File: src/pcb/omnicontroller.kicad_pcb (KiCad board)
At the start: 2 copper layers, 124.5 x 68.6 mm, 51 parts, among them J1 G-Switch GT-USB-7010ASV, U1 RP2040, U2 NCP1117ST33T3G, U3 W25Q128JVSIM, X1 SW_Omron_B3FS-1000P, Y1 ABM8-272-T3, Y2 SW_Omron_B3FS-1000P

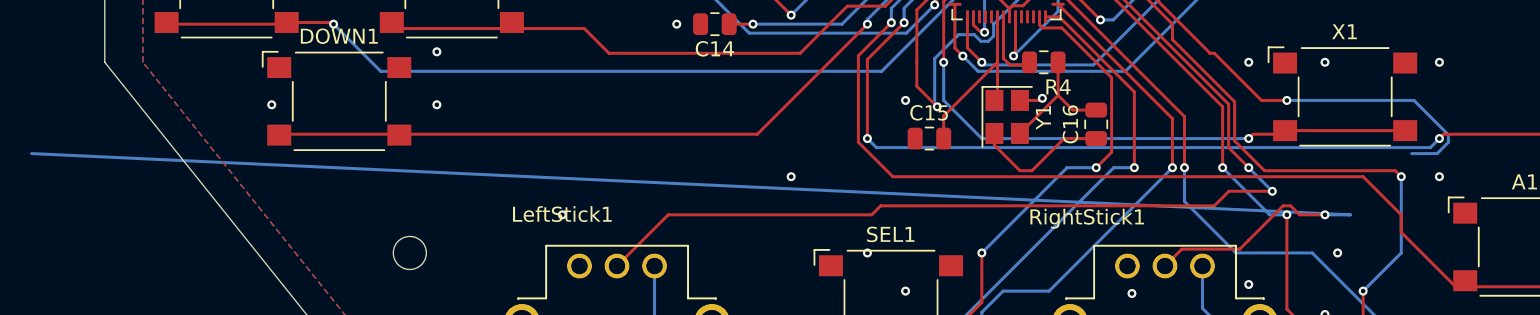
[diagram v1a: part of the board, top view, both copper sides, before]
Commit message: add RKJXV122400 footprint
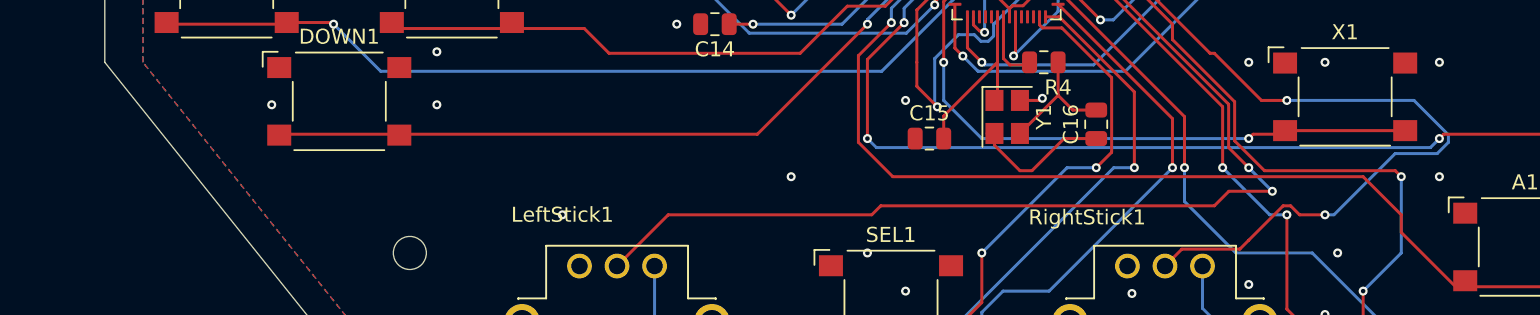
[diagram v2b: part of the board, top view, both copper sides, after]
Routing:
- net GP29: track 137.1 -> 54.9 mm
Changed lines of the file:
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@@
 			(drillshape 0)
 			(scaleselection 1)
-			(outputdirectory "../fabrication/v1.0.2/gerber/")
+			(outputdirectory "../../release/pcb/")
 		)
 	)
@@
 			(size 1 2.1)
 			(drill oval 0.6 1.7)
+			(property pad_prop_heatsink)
 			(layers "*.Cu" "*.Mask")
 			(remove_unused_layers no)
@@
 			(size 1 1.8)
 			(drill oval 0.6 1.4)
+			(property pad_prop_heatsink)
 			(layers "*.Cu" "*.Mask")
 			(remove_unused_layers no)
@@
 			(size 1 2.1)
 			(drill oval 0.6 1.7)
+			(property pad_prop_heatsink)
 			(layers "*.Cu" "*.Mask")
 			(remove_unused_layers no)
@@
 			(size 1 1.8)
 			(drill oval 0.6 1.4)
+			(property pad_prop_heatsink)
 			(layers "*.Cu" "*.Mask")
 			(remove_unused_layers no)
@@
 		)
 		(embedded_fonts no)
-		(model "${KICAD6_3DMODEL_DIR}/Connector_USB.3dshapes/USB_C_Receptacle_G-Switch_GT-USB-7010ASV.wrl"
+		(model "${KICAD9_3DMODEL_DIR}/Connector_USB.3dshapes/USB_C_Receptacle_G-Switch_GT-USB-7010ASV.wrl"
 			(offset
 				(xyz 0 0 0)
@@
 	(segment
 		(start 145.38 81.031471)
-		(end 145.38 81.528529)
+		(end 143.088529 78.74)
 		(width 0.2)
 		(layer "B.Cu")
@@
 	)
 	(segment
-		(start 143.088529 78.74)
-		(end 145.38 81.031471)
+		(start 144.628529 82.28)
+		(end 145.38 81.528529)
 		(width 0.2)
 		(layer "B.Cu")
@@
 	)
 	(segment
-		(start 144.628529 82.28)
-		(end 142.931471 82.28)
+		(start 143.088529 78.74)
+		(end 134.62 78.74)
 		(width 0.2)
 		(layer "B.Cu")
@@
 	)
 	(segment
-		(start 134.62 78.74)
-		(end 143.088529 78.74)
+		(start 145.38 81.528529)
+		(end 145.38 81.031471)
 		(width 0.2)
 		(layer "B.Cu")
@@
 	)
 	(segment
-		(start 145.38 81.528529)
-		(end 144.628529 82.28)
+		(start 137.75319 86.36)
+		(end 141.83319 82.28)
 		(width 0.2)
 		(layer "B.Cu")
@@
 	)
 	(segment
-		(start 51 82.28)
-		(end 138.851471 86.36)
+		(start 141.83319 82.28)
+		(end 144.628529 82.28)
 		(width 0.2)
 		(layer "B.Cu")
@@
 	)
 	(segment
-		(start 138.851471 86.36)
-		(end 137.16 86.36)
+		(start 137.16 86.36)
+		(end 137.75319 86.36)
 		(width 0.2)
 		(layer "B.Cu")

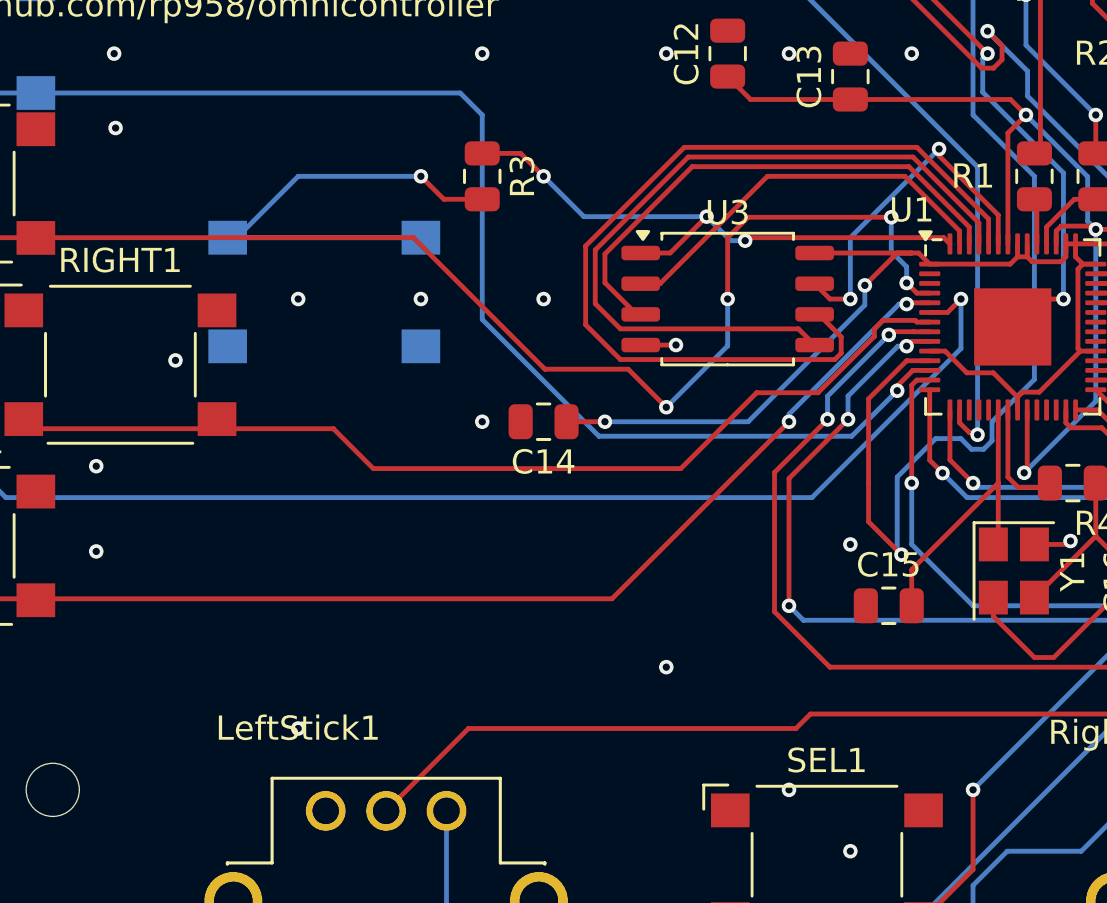
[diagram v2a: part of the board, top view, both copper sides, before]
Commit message: fix some drc warnings
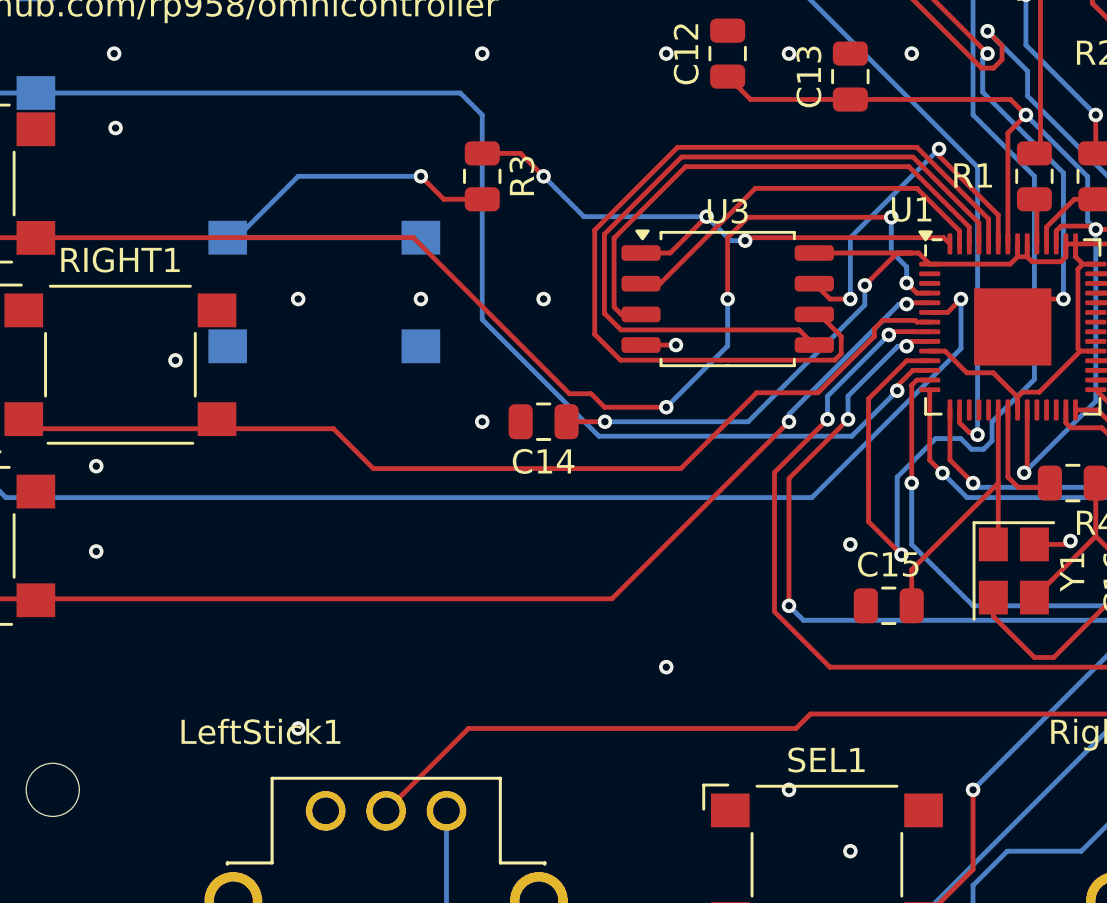
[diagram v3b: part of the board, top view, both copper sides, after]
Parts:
- U3: footprint Package_SO:SOIC-8_5.23x5.23mm_P1.27mm -> Package_SO:SOIC-8_5.3x5.3mm_P1.27mm

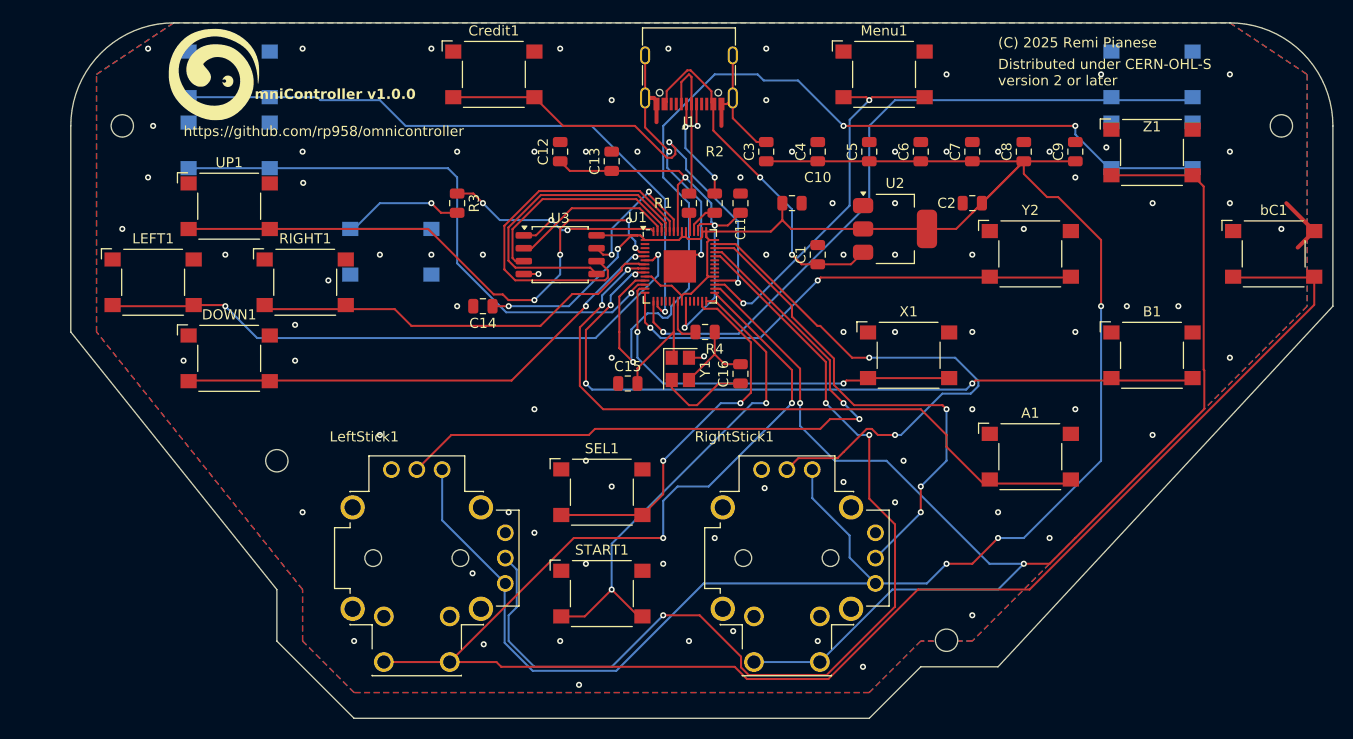
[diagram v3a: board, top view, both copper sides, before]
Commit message: move L1,L2, R1 and R2 buttons to top side
replace B3FS-1000 with B3F-3100 for those buttons
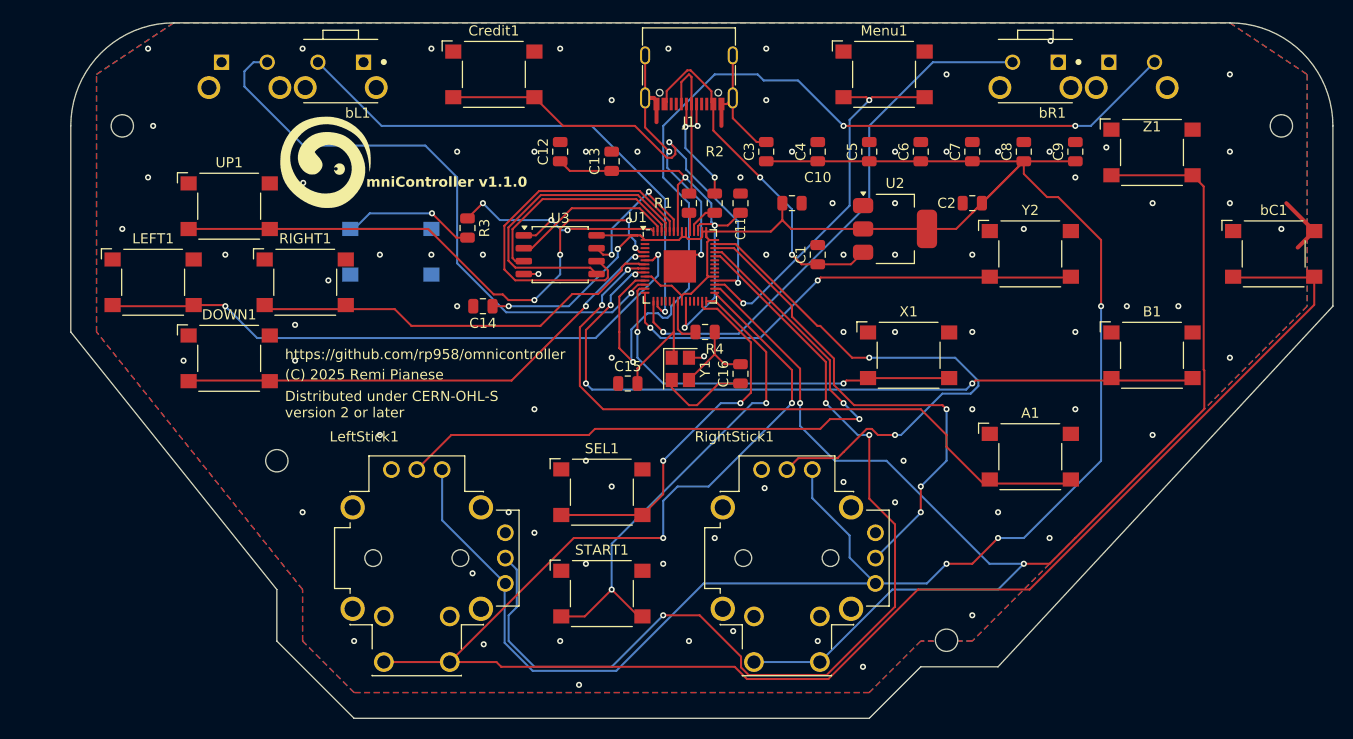
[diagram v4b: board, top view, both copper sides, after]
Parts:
- removed L1, L2: SW_Omron_B3FS-1000P, Button_Switch_SMD:SW_SPST_Omron_B3FS-100xP
- added bL1: SW_B3F-3100, Buttons:SW_B3F-3100, F.Cu at (82.5, 49.6)
- added bL2: SW_B3F-3100, Buttons:SW_B3F-3100, B.Cu at (73.0, 49.6)
- bR1: value SW_Omron_B3FS-1000P -> SW_B3F-3100; footprint Button_Switch_SMD:SW_SPST_Omron_B3FS-100xP -> Buttons:SW_B3F-3100; moved to F.Cu
- bR2: value SW_Omron_B3FS-1000P -> SW_B3F-3100; footprint Button_Switch_SMD:SW_SPST_Omron_B3FS-100xP -> Buttons:SW_B3F-3100
- moved G*** 14.0 mm to (81.0, 59.5)
- moved bR1 11.6 mm to (151.0, 49.6)
- moved bR2 8.44 mm to (160.5, 49.6), turned to 0 degrees
- moved R3 2.65 mm to (95.0, 66.0)
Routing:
- net GP12: track 69.8 -> 53.5 mm
- net GP13: track 63.6 -> 52.3 mm
- net GP08: track 97.4 -> 94.0 mm
- net GP09: track 57.1 -> 59.1 mm
- net Net-(BOOT_SEL1-Pad2): track 19.2 -> 20.4 mm
- net QSPI_SS: track 24.4 -> 23.6 mm
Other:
- board text added: "mniController v1.1.0"
- board text removed: "mniController v1.0.0"

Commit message: connect buttons C and Z to GPIO 22 and 23
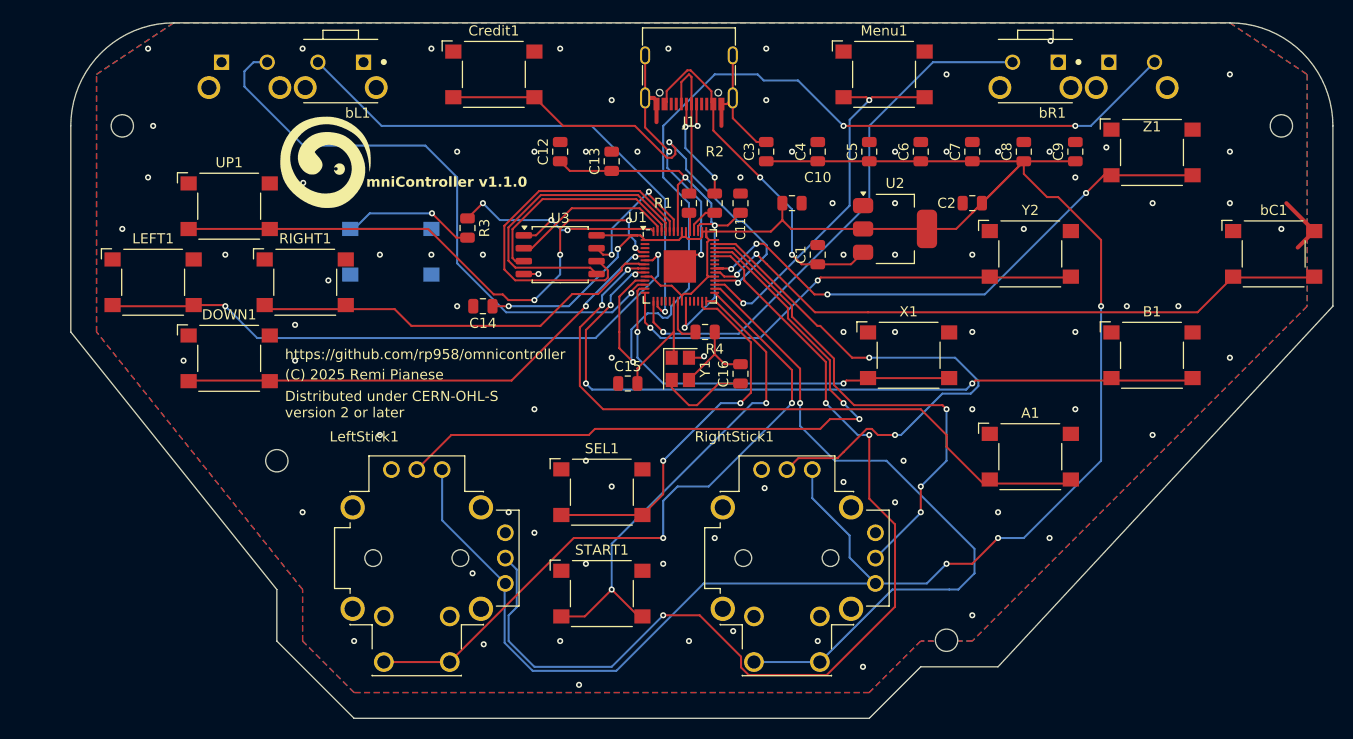
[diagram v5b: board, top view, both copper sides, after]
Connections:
- U1 pad 34: unconnected-(U1-GPIO22-Pad34) -> GP22
- U1 pad 35: unconnected-(U1-GPIO23-Pad35) -> GP23
- Z1 pad 2: GP19 -> GP23
- bC1 pad 2: GP18 -> GP22
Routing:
- net GP18: track 178.3 -> 67.0 mm
- net GP19: track 131.4 -> 67.3 mm, vias 2 -> 1
- net GP22: track 0.00 -> 63.4 mm, vias 0 -> 2
- net GP23: track 0.00 -> 55.9 mm, vias 0 -> 4
- net GP21: track 45.0 -> 47.6 mm
- net GP27: track 68.5 -> 69.1 mm
- net GP26: track 99.0 -> 99.6 mm

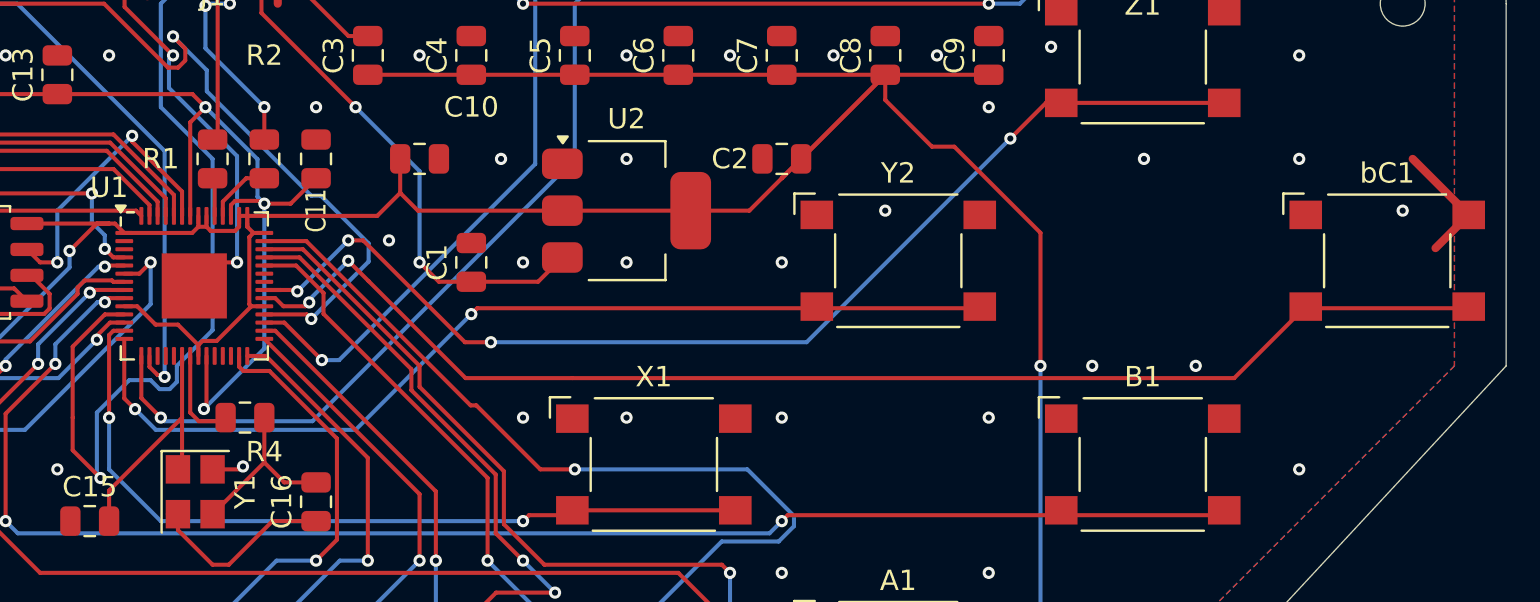
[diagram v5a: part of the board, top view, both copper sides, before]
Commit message: add USB A port for PS4/5 host mode authentication
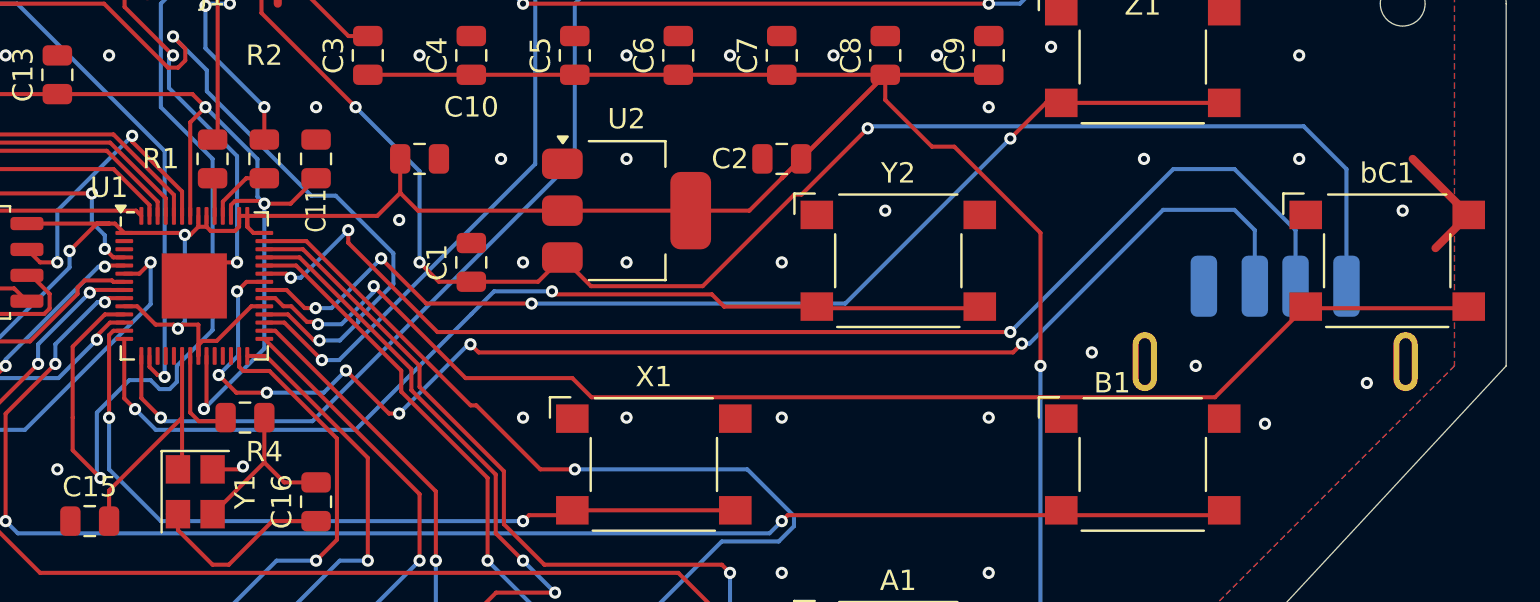
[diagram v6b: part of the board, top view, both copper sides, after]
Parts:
- added J2: USB_A, Connector_USB:USB_A_Receptacle_GCT_USB1046, B.Cu at (169.0, 77.0)
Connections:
- U1 pad 36: unconnected-(U1-GPIO24-Pad36) -> GP24
- U1 pad 37: unconnected-(U1-GPIO25-Pad37) -> GP25
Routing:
- net GP24: track 0.00 -> 66.4 mm, vias 0 -> 7
- net GP25: track 0.00 -> 61.4 mm, vias 0 -> 3
- net VBUS: track 34.8 -> 83.7 mm, vias 2 -> 3
- net GP21: track 47.6 -> 51.4 mm
- net +3V3: track 254.5 -> 257.1 mm, vias 5 -> 7
- net GP23: track 55.9 -> 53.5 mm
- net GP11: track 47.4 -> 48.7 mm
- net GP22: track 63.4 -> 64.0 mm
- net GND: vias 89 -> 90
